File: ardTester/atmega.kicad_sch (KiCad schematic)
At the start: 10 parts, among them U4 AMS1117-5.0, U5 ATmega328P-PU, Y1 Crystal

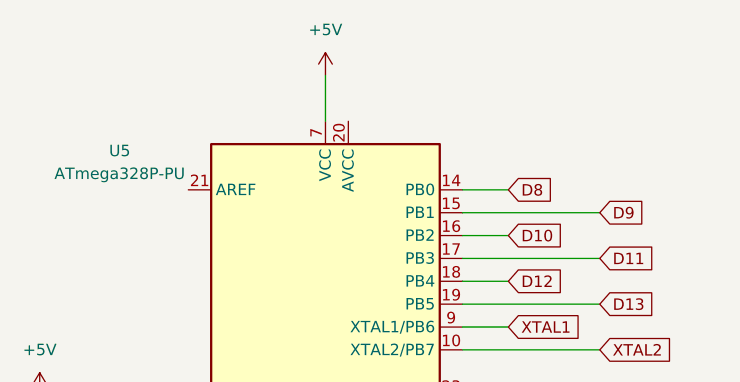
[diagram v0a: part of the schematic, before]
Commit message: atmega/arduino tester
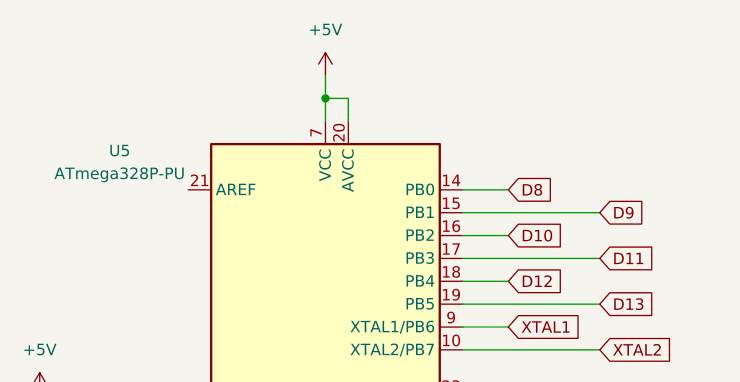
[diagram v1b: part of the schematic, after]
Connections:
- net +5V: now also U5.20 (AVCC)
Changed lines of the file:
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@@
   (junction (at 45.72 176.53) (diameter 0) (color 0 0 0 0)
   )
+  (junction (at 59.69 38.1) (diameter 0) (color 0 0 0 0)
+  )
   (junction (at 33.02 161.29) (diameter 0) (color 0 0 0 0)
   )
@@
     (stroke (width 0) (type default) (color 0 0 0 0))
   )
+  (wire (pts (xy 62.23 40.64) (xy 62.23 38.1))
+    (stroke (width 0) (type default) (color 0 0 0 0))
+  )
   (wire (pts (xy 118.11 156.21) (xy 118.11 161.29))
     (stroke (width 0) (type default) (color 0 0 0 0))
@@
     (stroke (width 0) (type default) (color 0 0 0 0))
   )
+  (wire (pts (xy 59.69 38.1) (xy 59.69 40.64))
+    (stroke (width 0) (type default) (color 0 0 0 0))
+  )
   (wire (pts (xy 74.93 86.36) (xy 100.33 86.36))
     (stroke (width 0) (type default) (color 0 0 0 0))
@@
     (stroke (width 0) (type default) (color 0 0 0 0))
   )
+  (wire (pts (xy 62.23 38.1) (xy 59.69 38.1))
+    (stroke (width 0) (type default) (color 0 0 0 0))
+  )
   (wire (pts (xy 74.93 91.44) (xy 80.01 91.44))
     (stroke (width 0) (type default) (color 0 0 0 0))
@@
     (stroke (width 0) (type default) (color 0 0 0 0))
   )
-  (wire (pts (xy 59.69 35.56) (xy 59.69 40.64))
+  (wire (pts (xy 59.69 35.56) (xy 59.69 38.1))
     (stroke (width 0) (type default) (color 0 0 0 0))
   )
@@
   (symbol (lib_id "power:GND") (at 62.23 121.92 0) (unit 1)
     (in_bom yes) (on_board yes) (fields_autoplaced)
-    (property "Reference" "#PWR0141" (id 0) (at 62.23 128.27 0)
+    (property "Reference" "#PWR041" (id 0) (at 62.23 128.27 0)
       (effects (font (size 1.27 1.27)) hide)
     )
@@
   (symbol (lib_id "power:+5V") (at 58.42 151.13 0) (unit 1)
     (in_bom yes) (on_board yes) (fields_autoplaced)
-    (property "Reference" "#PWR0135" (id 0) (at 58.42 154.94 0)
+    (property "Reference" "#PWR039" (id 0) (at 58.42 154.94 0)
       (effects (font (size 1.27 1.27)) hide)
     )
@@
   (symbol (lib_id "power:GND") (at 45.72 179.07 0) (unit 1)
     (in_bom yes) (on_board yes) (fields_autoplaced)
-    (property "Reference" "#PWR0136" (id 0) (at 45.72 185.42 0)
+    (property "Reference" "#PWR038" (id 0) (at 45.72 185.42 0)
       (effects (font (size 1.27 1.27)) hide)
     )
@@
   (symbol (lib_id "power:VCC") (at 33.02 151.13 0) (unit 1)
     (in_bom yes) (on_board yes) (fields_autoplaced)
-    (property "Reference" "#PWR0137" (id 0) (at 33.02 154.94 0)
+    (property "Reference" "#PWR037" (id 0) (at 33.02 154.94 0)
       (effects (font (size 1.27 1.27)) hide)
     )
@@
   (symbol (lib_id "power:+5V") (at 27.94 71.12 0) (unit 1)
     (in_bom yes) (on_board yes) (fields_autoplaced)
-    (property "Reference" "#PWR0142" (id 0) (at 27.94 74.93 0)
+    (property "Reference" "#PWR035" (id 0) (at 27.94 74.93 0)
       (effects (font (size 1.27 1.27)) hide)
     )
@@
   (symbol (lib_id "power:GND") (at 100.33 179.07 0) (unit 1)
     (in_bom yes) (on_board yes) (fields_autoplaced)
-    (property "Reference" "#PWR0138" (id 0) (at 100.33 185.42 0)
+    (property "Reference" "#PWR042" (id 0) (at 100.33 185.42 0)
       (effects (font (size 1.27 1.27)) hide)
     )
@@
   (symbol (lib_id "power:+5V") (at 113.03 80.01 0) (unit 1)
     (in_bom yes) (on_board yes) (fields_autoplaced)
-    (property "Reference" "#PWR0140" (id 0) (at 113.03 83.82 0)
+    (property "Reference" "#PWR043" (id 0) (at 113.03 83.82 0)
       (effects (font (size 1.27 1.27)) hide)
     )
@@
   (symbol (lib_id "power:+5V") (at 59.69 35.56 0) (unit 1)
     (in_bom yes) (on_board yes) (fields_autoplaced)
-    (property "Reference" "#PWR0139" (id 0) (at 59.69 39.37 0)
+    (property "Reference" "#PWR040" (id 0) (at 59.69 39.37 0)
       (effects (font (size 1.27 1.27)) hide)
     )
@@
   (symbol (lib_id "power:GND") (at 27.94 88.9 0) (unit 1)
     (in_bom yes) (on_board yes) (fields_autoplaced)
-    (property "Reference" "#PWR0143" (id 0) (at 27.94 95.25 0)
-      (effects (font (size 1.27 1.27)) hide)
-    )
+    (property "Reference" "#PWR036" (id 0) (at 27.94 95.25 0)
+      (effects (font (size 1.27 1.27)) hide)
+    )
